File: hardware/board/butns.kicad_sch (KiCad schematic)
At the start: 0 parts

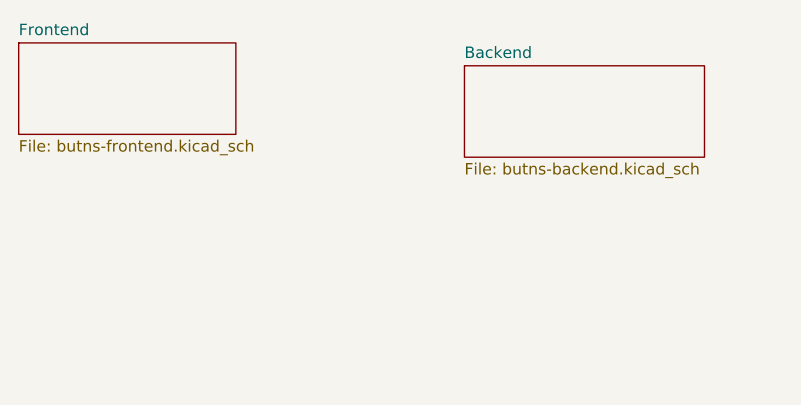
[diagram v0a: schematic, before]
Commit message: Convert to 16x8 grid (8 rows x 16 columns)
Hardware
- PCB extended to 190.44 x 99 mm with eight additional columns:
  128 switches, 128 diodes, 128 SK6812-EC20, 129 capacitors
- New column nets SW_COL_8..15 on GPIO16-22 and GPIO26, former
  SW_COL_8 (GPIO15) is now SW_COL_16
- LED chain runs row by row over 16 columns
- Tilt header J1 and I2C nets removed, GPIO27 left free
- Second inner mounting hole H6
- Schematic: new sheet butns-frontend2 with the 64 added cells,
  frontend and backend sheets adapted
- Regenerated jlcpcb/ gerbers, BOM and CPL, new butns.step,
  removed stale 8x8 butns.stl and model/butns.wrl

Firmware
- 16 column matrix scan per column with settle time
- LED index row * 16 + col, rotation limited to 0 and 180 degrees
- LED current estimate limited to MAX_LED_CURRENT_MA
- MPU6050 tilt support removed
- Fix led/level/row and led/level/col offset handling

Case
- case.scad and buttons.scad extended to 16 columns, second standoff
- Explicit apply_to argument for roundedcube calls

Co-Authored-By: Claude Opus 5.5 <noreply@anthropic.com>
Claude-Session: https://claude.ai/code/session_0195H63MEXeeVZ7CNyHAeb6N
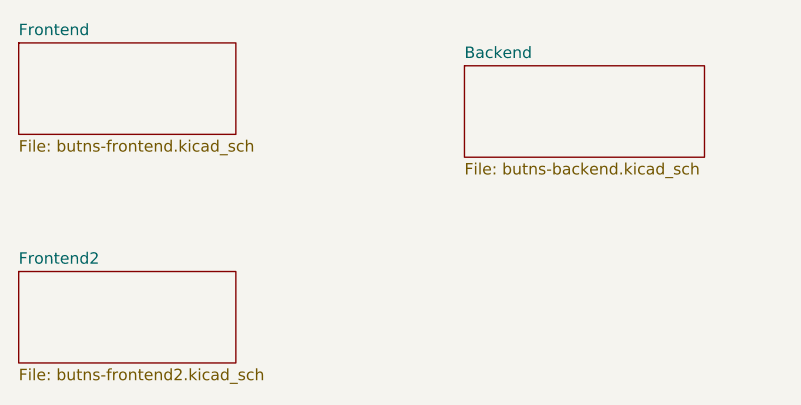
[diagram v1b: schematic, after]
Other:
- added sheet Frontend2 (butns-frontend2.kicad_sch)
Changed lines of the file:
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@@
+		)
+	)
+	(sheet
+		(at 128.27 100.33)
+		(size 24.13 10.16)
+		(fields_autoplaced yes)
+		(stroke
+			(width 0.1524)
+			(type solid)
+		)
+		(fill
+			(color 0 0 0 0.0000)
+		)
+		(property "Sheetname" "Frontend2"
+			(at 128.27 99.6184 0)
+			(effects
+				(font
+					(size 1.27 1.27)
+				)
+				(justify left bottom)
+			)
+		)
+		(property "Sheetfile" "butns-frontend2.kicad_sch"
+			(at 128.27 111.0746 0)
+			(effects
+				(font
+					(size 1.27 1.27)
+				)
+				(justify left top)
+			)
+		)
+		(instances
+			(project "butns"
+				(path "/1c3520c0-bca7-4d12-8c9b-3ac18c44338d"
+					(page "4")
+				)
+			)
 		)
 	)
